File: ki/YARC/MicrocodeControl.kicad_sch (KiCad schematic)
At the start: 0 parts

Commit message: Significant progress on microcode schematic. Minor improvements to MemorySystem.md.
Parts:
- added U? (x15): 74LS32, symbol 74xx:74LS32
- added U? (x3): 74LS157, symbol 74xx:74LS157
- added U? (x2): 74LS574, symbol 74xx:74LS574
- added U? (x2): 74LS193, symbol 74xx:74LS193
- added U? (x2): 74LS139, symbol 74xx_IEEE:74LS139
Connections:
- new net: U?.2, U?.9 (Zc)
- new net: U?.1 (S), U?.1 (S), U?.12 (Q7)
- new net: U?.10 (I1c), U?.17 (Q2)
- new net: U?.13 (I1d), U?.16 (Q3)
- new net: U?.19 (Q0), U?.3 (I1a)
- new net: U?.18 (Q1), U?.6 (I1b)
- new net: U?.2, U?.7 (~{Q3})
- new net: U?.12 (Zd), U?.2
- new net: U?.11 (I0c), U?.6 (~{Q2})
- new net: U?.14 (I0d), U?.7 (~{Q3})
- new net: U?.2 (I0a), U?.4 (~{Q0})
- new net: U?.2, U?.4 (Za)
- new net: U?.5 (I0b), U?.5 (~{Q1})
- new net: U?.2, U?.7 (Zb)
- new net: U?.1 (~{EN}), U?.13 (Q6)
- new net: U?.14 (Q5), U?.3 (B)
- new net: U?.15 (Q4), U?.2 (A)
- new net: U?.1 (~{EN}), U?.17 (Q2)
- new net: U?.18 (Q1), U?.3 (B)
- new net: U?.19 (Q0), U?.2 (A)
- new net: U?.12 (~{CO}), U?.5 (UP)
- new net: U?.2, U?.4 (~{Q0})
- new net: U?.10 (I1c), U?.13 (Q6)
- new net: U?.15 (Q4), U?.3 (I1a)
- new net: U?.14 (Q5), U?.6 (I1b)
- new net: U?.2, U?.6 (~{Q2})
- new net: U?.2, U?.5 (~{Q1})
- new net GND: U?.1 (B), U?.1 (B), U?.1 (OE), U?.10 (C), U?.10 (C), U?.10 (GND), U?.10 (GND), U?.10 (I1c), U?.13 (I1d), U?.13 (I1d), U?.14 (CLR), U?.14 (CLR), U?.15 (A), U?.15 (A), U?.15 (E), U?.15 (E), U?.3 (I1a), U?.6 (I1b), U?.8 (GND), U?.8 (GND), U?.8 (GND), U?.8 (GND), U?.8 (GND), U?.8 (GND), U?.8 (GND), U?.9 (D), U?.9 (D)
- new net IRCLK: U?.11 (Cp), U?.11 (~{LOAD}), U?.11 (~{LOAD})
- new net IRL-0: U?.2 (I0a)
- new net KA0: U?.3 (QA)
- new net KA1: U?.2 (QB)
- new net KA10: U?.4 (Za)
- new net KA11: U?.7 (Zb)
- new net KA12: U?.9 (Zc)
- new net KA2: U?.6 (QC)
- new net KA3: U?.7 (QD)
- new net KA4: U?.3 (QA)
- new net KA5: U?.2 (QB)
- new net KA6: U?.4 (Za)
- new net KA7: U?.7 (Zb)
- new net KA8: U?.9 (Zc)
- new net KA9: U?.12 (Zd)
- new net KCLK0: U?.3, U?.3, U?.3, U?.3
- new net KX0: U?.2 (D0)
- new net KX7: U?.9 (D7)
- new net SYSBUS15: U?.9 (D7)
- new net SYSBUS8: U?.2 (D0)
- new net SYSBUS:15: U?.1, U?.1, U?.2, U?.2
- new net SYSCLK: U?.1, U?.1, U?.1, U?.1, U?.1, U?.1, U?.1, U?.1, U?.5 (UP)
- new net UCCLK: U?.11 (Cp)
- new net VCC: U?.11 (I0c), U?.11 (I0c), U?.14 (I0d), U?.14 (I0d), U?.16 (VCC), U?.16 (VCC), U?.16 (VCC), U?.16 (VCC), U?.16 (VCC), U?.16 (VCC), U?.16 (VCC), U?.2 (I0a), U?.20 (VCC), U?.20 (VCC), U?.4 (DOWN), U?.4 (DOWN), U?.5 (I0b), U?.5 (I0b)
- new net ~{KI0EN}: U?.2, U?.3
- new net ~{KI1EN}: U?.2, U?.3
- new net ~{KI2EN}: U?.1, U?.3
- new net ~{KI3EN}: U?.1, U?.3
- new net ~{UC_WE0}: U?.3
- new net ~{UC_WE1}: U?.3
- new net ~{UC_WE2}: U?.3
- new net ~{UC_WE3}: U?.3
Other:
- note added: "IR HIGH (IRH)"
- note added: "MICROCODE CONTROL REGISTER"

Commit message: Continue with microcode schematic
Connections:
- net GND: now also U?.15 (E); no longer U?.14 (CLR)
- net VCC: now also U?.1 (OE)
- net IRH15: now reaches U?.1 (S), U?.1 (S), U?.12 (Q7)
- net IRH10: now reaches U?.10 (I1c), U?.17 (Q2)
- net IRH11: now reaches U?.13 (I1d), U?.16 (Q3)
- net IRH8: now reaches U?.19 (Q0), U?.3 (I1a)
- net IRH9: now reaches U?.18 (Q1), U?.6 (I1b)
- net YARC/~{NANO}: now reaches U?.1 (S)
- net KX1: now reaches U?.3 (D1)
- net KX2: now reaches U?.4 (D2)
- net KX3: now reaches U?.5 (D3)
- net KX4: now reaches U?.6 (D4)
- net KX5: now reaches U?.7 (D5)
- net KX6: now reaches U?.8 (D6)
- net IRH14: now reaches U?.10 (I1c), U?.13 (Q6)
- net IRH12: now reaches U?.15 (Q4), U?.3 (I1a)
- net IRH13: now reaches U?.14 (Q5), U?.6 (I1b)
- net SYSDATA9: now reaches U?.3 (D1)
- net SYSDATA10: now reaches U?.4 (D2)
- net SYSDATA11: now reaches U?.5 (D3)
- net SYSDATA12: now reaches U?.6 (D4)
- net SYSDATA13: now reaches U?.7 (D5)
- net SYSDATA14: now reaches U?.8 (D6)
- net IRL-0 renamed IRL0
- net SYSBUS15 renamed SYSDATA15
- net SYSBUS8 renamed SYSDATA8
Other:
- note added: "ALSO ON SHT 8"
- moved on the sheet: U?

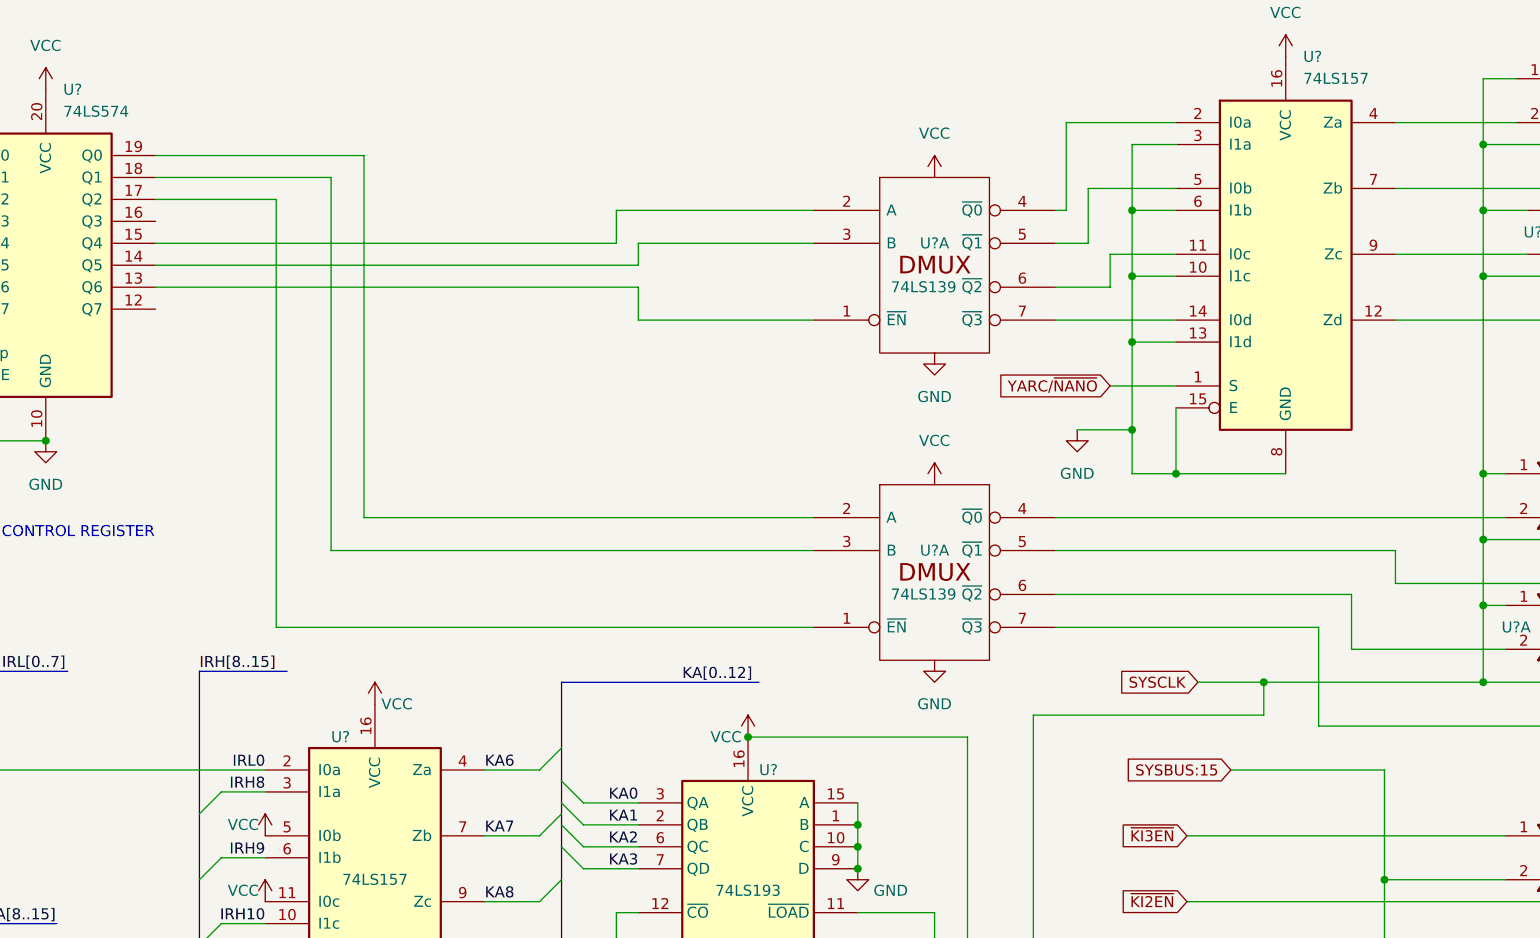
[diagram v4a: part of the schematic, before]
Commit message: Fixing wiring diagram and implement writeToK()
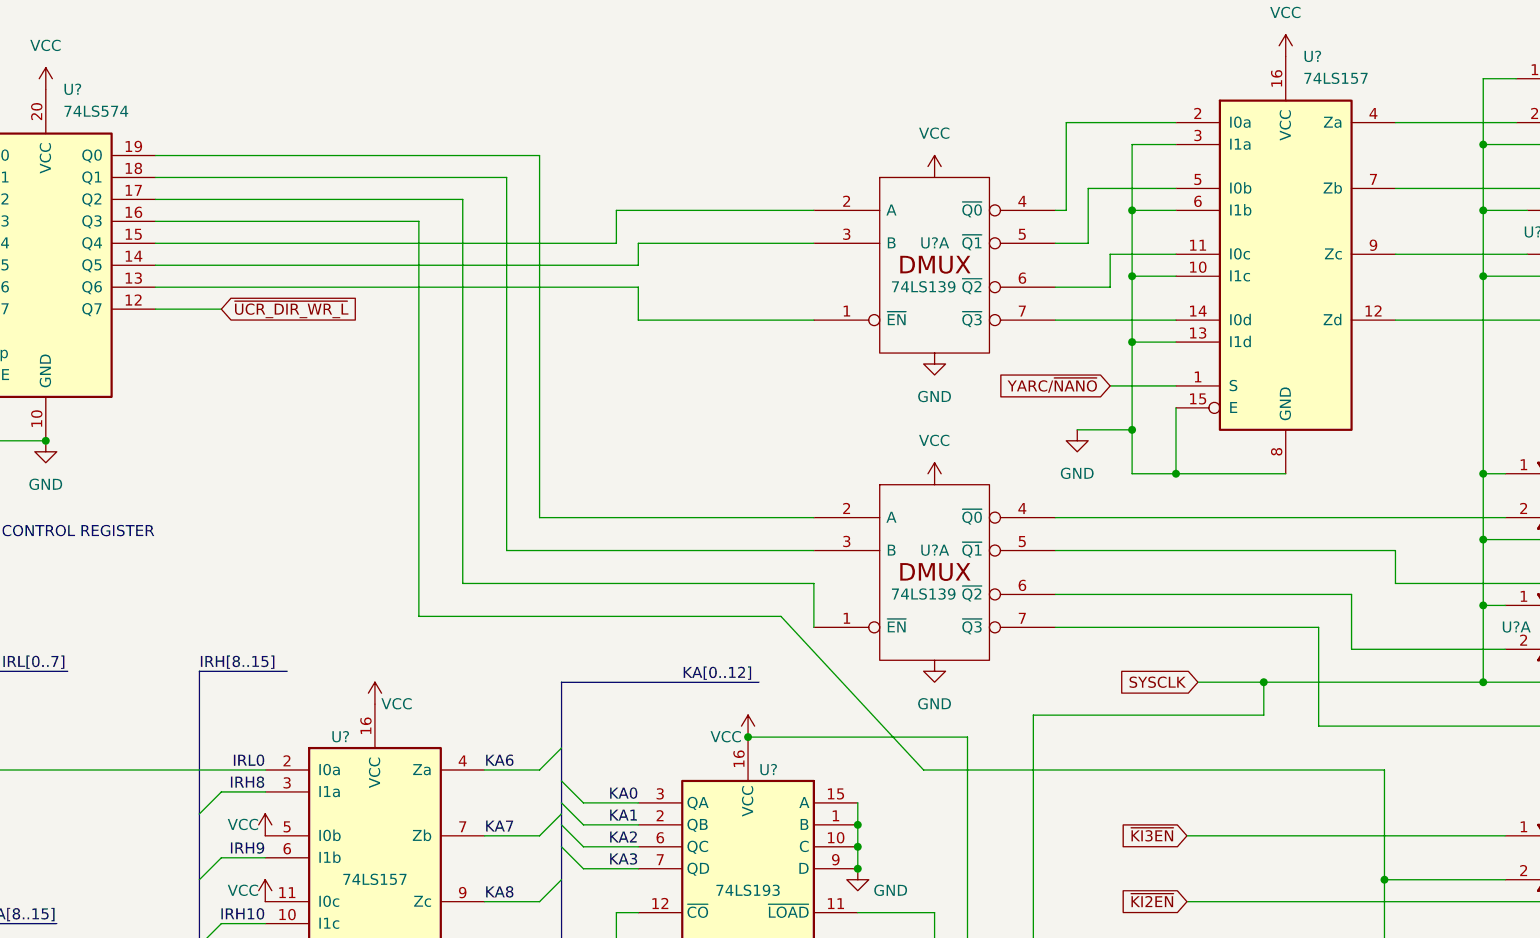
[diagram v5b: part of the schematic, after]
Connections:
- net SYSBUS:15 is gone; now on an unnamed net: U?.1, U?.1, U?.2, U?.2
- net ~{UCR_DIR_WR_L}: now reaches U?.12 (Q7)
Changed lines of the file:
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@@
     (stroke (width 0) (type default) (color 0 0 0 0))
   )
-  (wire (pts (xy 55.88 33.02) (xy 76.2 33.02))
+  (wire (pts (xy 55.88 33.02) (xy 96.52 33.02))
     (stroke (width 0) (type default) (color 0 0 0 0))
   )
@@
     (stroke (width 0) (type default) (color 0 0 0 0))
   )
+  (wire (pts (xy 55.88 38.1) (xy 86.36 38.1))
+    (stroke (width 0) (type default) (color 0 0 0 0))
+  )
   (wire (pts (xy 209.55 44.45) (xy 209.55 36.83))
     (stroke (width 0) (type default) (color 0 0 0 0))
@@
     (stroke (width 0) (type default) (color 0 0 0 0))
   )
-  (wire (pts (xy 69.85 35.56) (xy 69.85 85.09))
-    (stroke (width 0) (type default) (color 0 0 0 0))
-  )
   (wire (pts (xy 22.86 160.02) (xy 24.13 160.02))
     (stroke (width 0) (type default) (color 0 0 0 0))
@@
     (stroke (width 0) (type default) (color 0 0 0 0))
   )
+  (wire (pts (xy 55.88 48.26) (xy 63.5 48.26))
+    (stroke (width 0) (type default) (color 0 0 0 0))
+  )
   (wire (pts (xy 137.16 125.73) (xy 149.86 125.73))
     (stroke (width 0) (type default) (color 0 0 0 0))
@@
     (stroke (width 0) (type default) (color 0 0 0 0))
   )
+  (wire (pts (xy 132.08 85.09) (xy 132.08 80.01))
+    (stroke (width 0) (type default) (color 0 0 0 0))
+  )
   (wire (pts (xy 227.33 111.76) (xy 245.11 111.76))
     (stroke (width 0) (type default) (color 0 0 0 0))
   )
-  (wire (pts (xy 80.01 30.48) (xy 80.01 72.39))
-    (stroke (width 0) (type default) (color 0 0 0 0))
-  )
   (wire (pts (xy 58.42 147.32) (xy 53.34 147.32))
     (stroke (width 0) (type default) (color 0 0 0 0))
@@
     (stroke (width 0) (type default) (color 0 0 0 0))
   )
+  (wire (pts (xy 86.36 38.1) (xy 86.36 83.82))
+    (stroke (width 0) (type default) (color 0 0 0 0))
+  )
   (wire (pts (xy 212.09 82.55) (xy 209.55 82.55))
     (stroke (width 0) (type default) (color 0 0 0 0))
@@
     (stroke (width 0) (type default) (color 0 0 0 0))
   )
+  (wire (pts (xy 86.36 83.82) (xy 128.27 83.82))
+    (stroke (width 0) (type default) (color 0 0 0 0))
+  )
   (wire (pts (xy 175.26 116.84) (xy 226.06 116.84))
     (stroke (width 0) (type default) (color 0 0 0 0))
@@
     (stroke (width 0) (type default) (color 0 0 0 0))
   )
+  (wire (pts (xy 96.52 76.2) (xy 132.08 76.2))
+    (stroke (width 0) (type default) (color 0 0 0 0))
+  )
   (wire (pts (xy 16.51 154.94) (xy 27.94 154.94))
     (stroke (width 0) (type default) (color 0 0 0 0))
@@
     (stroke (width 0) (type default) (color 0 0 0 0))
   )
+  (wire (pts (xy 100.33 72.39) (xy 132.08 72.39))
+    (stroke (width 0) (type default) (color 0 0 0 0))
+  )
   (wire (pts (xy 160.02 40.64) (xy 163.83 40.64))
     (stroke (width 0) (type default) (color 0 0 0 0))
@@
     (stroke (width 0) (type default) (color 0 0 0 0))
   )
-  (wire (pts (xy 180.34 101.6) (xy 198.12 101.6))
+  (wire (pts (xy 144.78 101.6) (xy 198.12 101.6))
     (stroke (width 0) (type default) (color 0 0 0 0))
   )
@@
     (stroke (width 0) (type default) (color 0 0 0 0))
   )
-  (wire (pts (xy 76.2 33.02) (xy 76.2 76.2))
-    (stroke (width 0) (type default) (color 0 0 0 0))
-  )
   (wire (pts (xy 175.26 129.54) (xy 212.09 129.54))
     (stroke (width 0) (type default) (color 0 0 0 0))
@@
     (stroke (width 0) (type default) (color 0 0 0 0))
   )
+  (wire (pts (xy 91.44 80.01) (xy 132.08 80.01))
+    (stroke (width 0) (type default) (color 0 0 0 0))
+  )
   (wire (pts (xy 168.91 44.45) (xy 168.91 36.83))
     (stroke (width 0) (type default) (color 0 0 0 0))
@@
     (stroke (width 0) (type default) (color 0 0 0 0))
   )
-  (wire (pts (xy 80.01 72.39) (xy 132.08 72.39))
+  (wire (pts (xy 91.44 35.56) (xy 91.44 80.01))
     (stroke (width 0) (type default) (color 0 0 0 0))
   )
@@
     (stroke (width 0) (type default) (color 0 0 0 0))
   )
+  (wire (pts (xy 128.27 83.82) (xy 144.78 101.6))
+    (stroke (width 0) (type default) (color 0 0 0 0))
+  )
   (wire (pts (xy 209.55 21.59) (xy 209.55 29.21))
     (stroke (width 0) (type default) (color 0 0 0 0))
@@
     (stroke (width 0) (type default) (color 0 0 0 0))
   )
-  (wire (pts (xy 76.2 76.2) (xy 132.08 76.2))
-    (stroke (width 0) (type default) (color 0 0 0 0))
-  )
   (wire (pts (xy 160.02 85.09) (xy 190.5 85.09))
     (stroke (width 0) (type default) (color 0 0 0 0))
@@
     (stroke (width 0) (type default) (color 0 0 0 0))
   )
-  (wire (pts (xy 69.85 85.09) (xy 132.08 85.09))
-    (stroke (width 0) (type default) (color 0 0 0 0))
-  )
   (wire (pts (xy 16.51 152.4) (xy 27.94 152.4))
     (stroke (width 0) (type default) (color 0 0 0 0))
@@
     (stroke (width 0) (type default) (color 0 0 0 0))
   )
-  (wire (pts (xy 55.88 30.48) (xy 80.01 30.48))
+  (wire (pts (xy 55.88 30.48) (xy 100.33 30.48))
     (stroke (width 0) (type default) (color 0 0 0 0))
   )
@@
     (stroke (width 0) (type default) (color 0 0 0 0))
   )
+  (wire (pts (xy 96.52 33.02) (xy 96.52 76.2))
+    (stroke (width 0) (type default) (color 0 0 0 0))
+  )
   (wire (pts (xy 173.99 59.69) (xy 173.99 67.31))
     (stroke (width 0) (type default) (color 0 0 0 0))
@@
     (stroke (width 0) (type default) (color 0 0 0 0))
   )
+  (wire (pts (xy 100.33 30.48) (xy 100.33 72.39))
+    (stroke (width 0) (type default) (color 0 0 0 0))
+  )
   (wire (pts (xy 105.41 113.03) (xy 111.76 113.03))
     (stroke (width 0) (type default) (color 0 0 0 0))
@@
     (stroke (width 0) (type default) (color 0 0 0 0))
   )
-  (wire (pts (xy 55.88 35.56) (xy 69.85 35.56))
+  (wire (pts (xy 55.88 35.56) (xy 91.44 35.56))
     (stroke (width 0) (type default) (color 0 0 0 0))
   )
@@
   (label "KX3" (at 30.48 38.1 180)
     (effects (font (size 1.27 1.27)) (justify right bottom))
-  )
-  (global_label "SYSBUS:15" (shape input) (at 180.34 101.6 180) (fields_autoplaced)
-    (effects (font (size 1.27 1.27)) (justify right))
-    (property "Intersheet References" "${INTERSHEET_REFS}" (id 0) (at 167.5855 101.5206 0)
-      (effects (font (size 1.27 1.27)) (justify right) hide)
-    )
   )
   (global_label "~{KI3EN}" (shape input) (at 175.26 109.22 180) (fields_autoplaced)
@@
     )
   )
+  (global_label "~{UCR_DIR_WR_L}" (shape input) (at 63.5 48.26 0) (fields_autoplaced)
+    (effects (font (size 1.27 1.27)) (justify left))
+    (property "Intersheet References" "${INTERSHEET_REFS}" (id 0) (at 79.5807 48.1806 0)
+      (effects (font (size 1.27 1.27)) (justify left) hide)
+    )
+  )

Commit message: Ongoing development of registers and ALU
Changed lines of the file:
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@@
+    (stroke (width 0) (type default) (color 0 0 0 0))
+  )
+  (wire (pts (xy 137.16 184.15) (xy 137.16 190.5))
     (stroke (width 0) (type default) (color 0 0 0 0))
   )
@@
     (stroke (width 0) (type default) (color 0 0 0 0))
   )
+  (wire (pts (xy 124.46 190.5) (xy 137.16 190.5))
+    (stroke (width 0) (type default) (color 0 0 0 0))
+  )
